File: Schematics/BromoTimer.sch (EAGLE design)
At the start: 30 parts, among them IC1 PIC16F687, IC2 7805TV, K1 G2R2A, K2 G2R2A, Q1 BC548B, Q2 BC548B, Q3 BC548B, X1 AC_IN, X4 22-23-2041, X5 AC_OUT

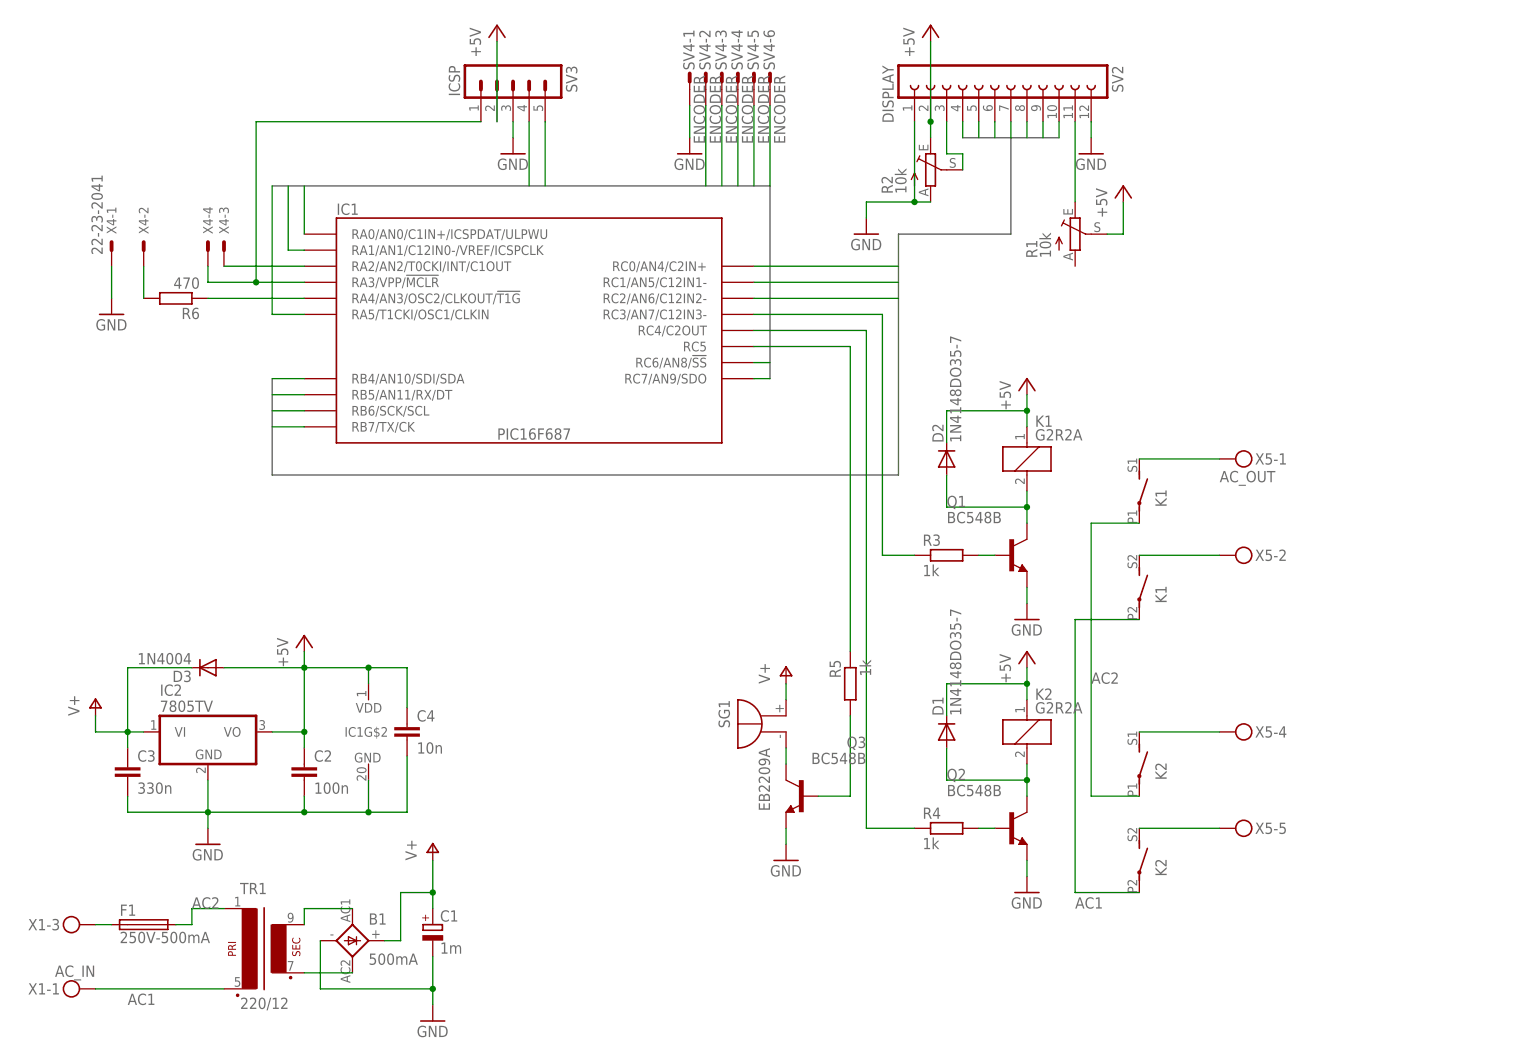
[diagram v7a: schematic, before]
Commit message: Use piezo instead of buzzer, add mounting holes
Use piezo instead of a buzzer so we save a resistor and a transistor. The piezo
will ring via PWM by the PIC. Re-routed portions of the PCB for a better fit.
Add mounting holes to PCB.
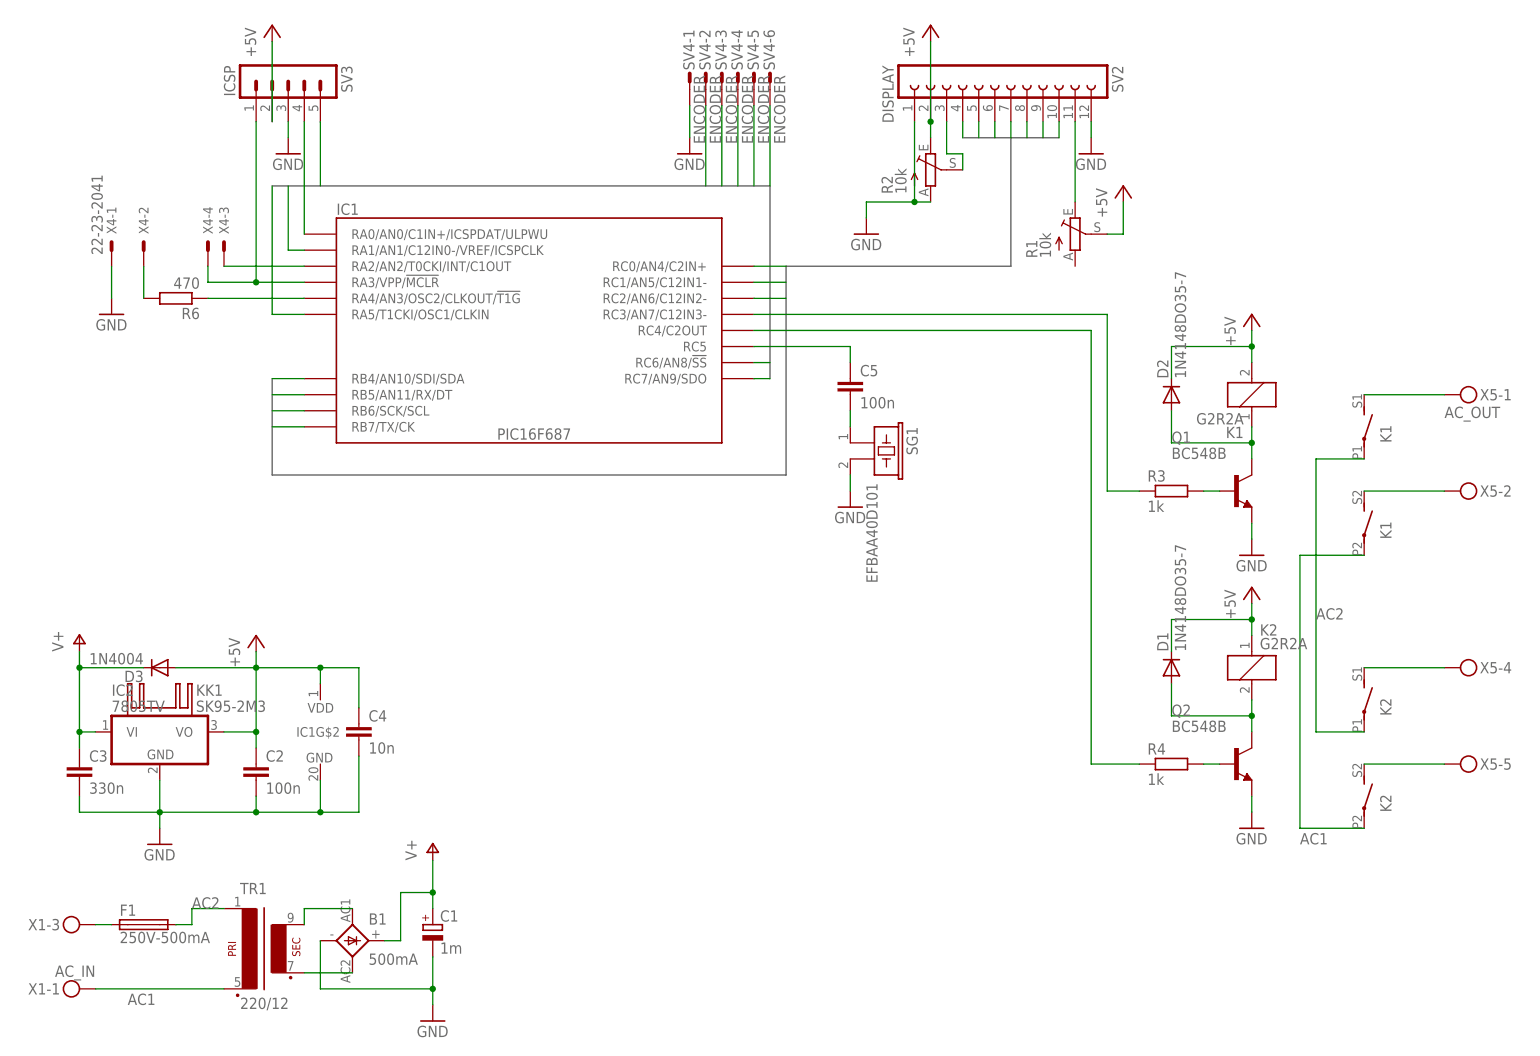
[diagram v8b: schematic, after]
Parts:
- removed Q3: BC548B, transistor-npn:BC548B
- removed R5: 1k, rcl:R-EU_0207/10
- added C5: 100n, rcl:C-EU075-032X103
- added KK1: SK95-2M3, heatsink:SK95-2M3
- R3, R4, R6: device rcl:R-EU_0207/10 -> rcl:R-EU_0207/7
- SG1: value EB2209A -> EFBAA40D101; device buzzer:EB2209A -> buzzer:EFBAA40D101
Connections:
- removed net N$19: Q3.C, SG1.-
- net +5V: now also K11.2; no longer K11.1
- net GND: now also SG1.2; no longer Q3.E
- net N$17: now also C5.1; no longer R5.1
- net N$18: now also C5.2, SG1.1; no longer Q3.B, R5.2
- net N$7: now also K11.1; no longer K11.2
- net V+: no longer SG1.+
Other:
- moved on the sheet: C2, C3, C4, D1, D2, D3, IC1G$2, IC2, K1, K2, Q1, Q2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
